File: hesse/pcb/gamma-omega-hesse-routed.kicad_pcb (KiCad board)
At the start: 2 copper layers, 232.8 x 111.4 mm, 47 parts

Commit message: Remove duplicated automated traces from Ergogen
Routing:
- net C2: track 294.8 -> 212.9 mm
- net C1: track 301.4 -> 225.6 mm
- net C4: track 256.1 -> 180.2 mm
- net C11: track 294.1 -> 218.3 mm
- net C5: track 185.3 -> 109.4 mm
- net C10: track 229.9 -> 154.1 mm
- net C12: track 306.4 -> 230.5 mm
- net C3: track 218.2 -> 142.4 mm
- net R7: track 406.8 -> 334.3 mm
- net R5: track 566.2 -> 493.7 mm
- net R1: track 270.0 -> 197.6 mm
- net R8: track 380.6 -> 308.2 mm
- net R3: track 396.1 -> 323.7 mm
- net R2: track 469.0 -> 396.6 mm
- net R9: track 339.2 -> 266.8 mm
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
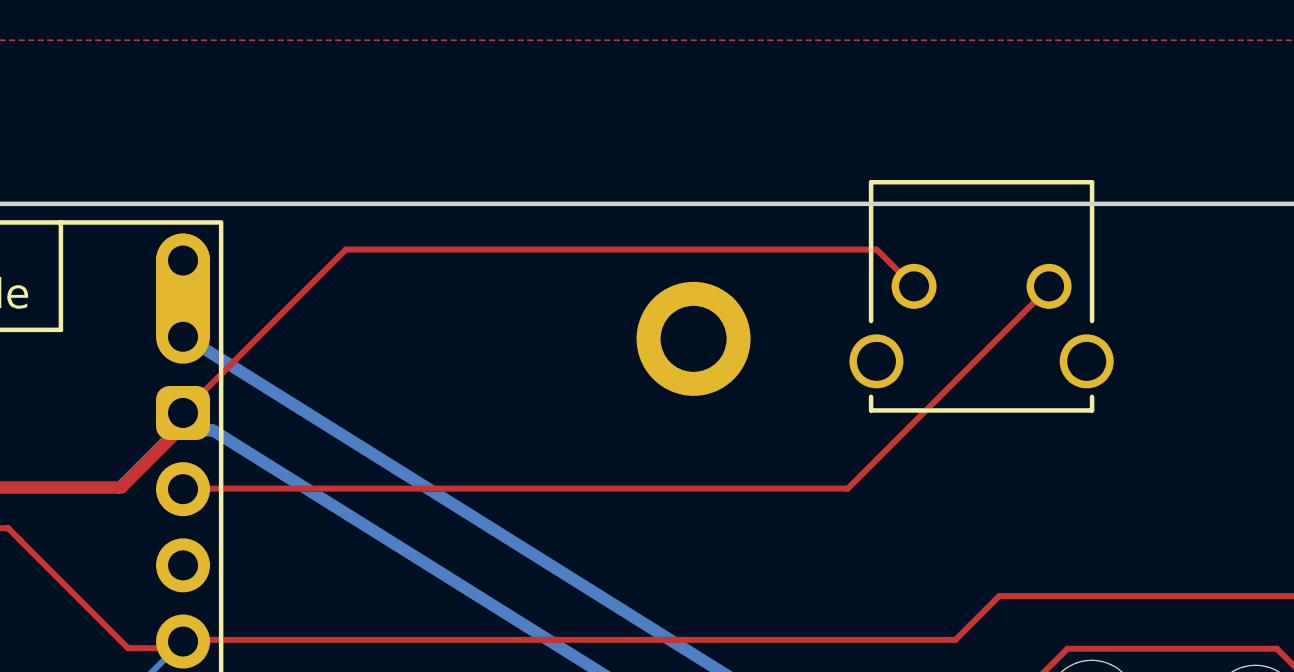
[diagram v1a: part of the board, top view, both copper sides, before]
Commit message: Move Hesse reset switch 1mm in (for case clearance)
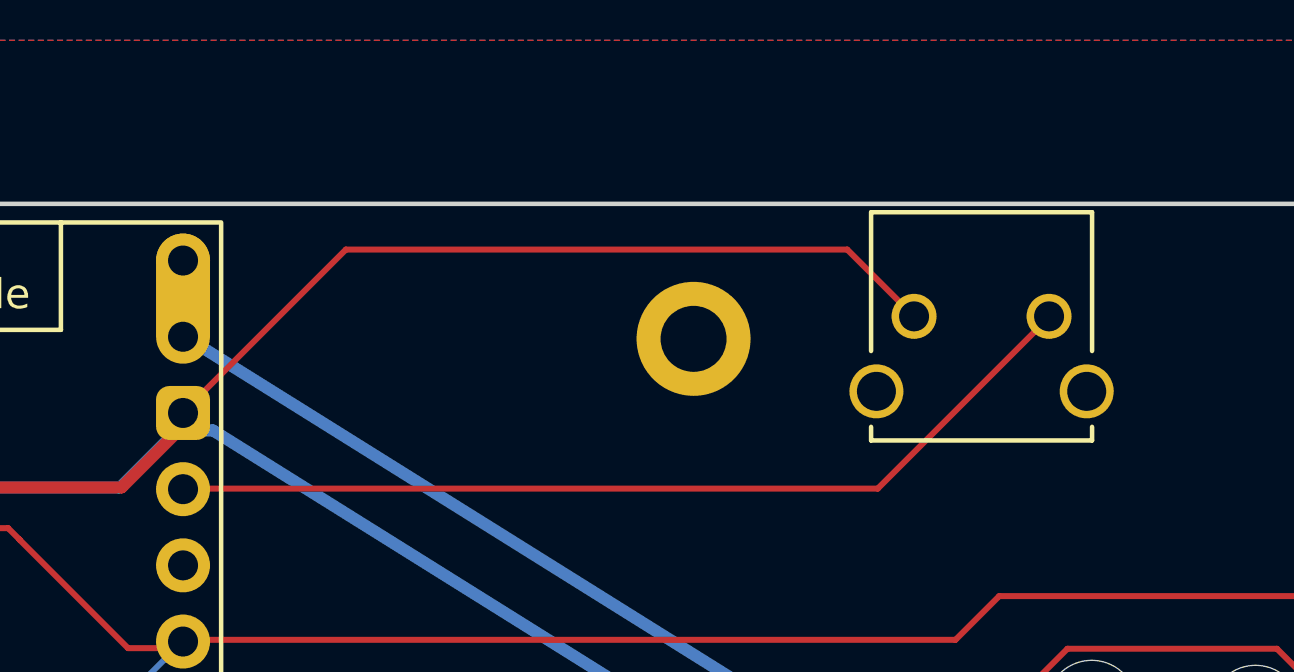
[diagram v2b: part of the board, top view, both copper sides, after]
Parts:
- moved RST1 1.00 mm to (193.1, 53.5)
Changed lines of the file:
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@@
 	(footprint "peterjc:reset_switch_1825027-8"
 		(layer "F.Cu")
-		(at 193.137923 52.5 180)
+		(at 193.137923 53.5 180)
 		(property "Reference" "RST1"
 			(at 0 2.55 270)
@@
 	)
 	(segment
-		(start 188.598386 52.481019)
-		(end 187.39101 51.273637)
-		(width 0.2)
-		(layer "F.Cu")
-		(net 3)
-	)
-	(segment
 		(start 169.697082 51.27364)
-		(end 164.268829 56.701896)
+		(end 186.411563 51.27364)
 		(width 0.2)
 		(layer "F.Cu")
@@
 	)
 	(segment
-		(start 187.39101 51.273637)
-		(end 169.697082 51.27364)
+		(start 188.637923 53.5)
+		(end 186.411563 51.27364)
 		(width 0.2)
 		(layer "F.Cu")
@@
 		(net 3)
 	)
+	(segment
+		(start 169.697082 51.27364)
+		(end 164.268829 56.701896)
+		(width 0.2)
+		(layer "F.Cu")
+		(net 3)
+	)
 	(via
 		(at 189.780327 122.563278)
@@
 	)
 	(segment
-		(start 186.429396 59.241905)
-		(end 193.189547 52.481753)
+		(start 187.428084 59.241916)
+		(end 193.189547 53.480453)
 		(width 0.2)
 		(layer "F.Cu")
@@
 	(segment
 		(start 164.268861 59.241916)
-		(end 186.429396 59.241905)
+		(end 187.428084 59.241916)
 		(width 0.2)
 		(layer "F.Cu")
